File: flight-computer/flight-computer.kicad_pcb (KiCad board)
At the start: 2 copper layers, 25.4 x 50.8 mm, 29 parts, among them J1 USB_C_Receptacle_USB2.0_16P, J2 MEM2067-02-180-00-A, Q1 DMN3404L, Q2 DMN3404L, SW1 Reset, SW2 Boot, U1 LMR51420X, U2 ESP32-S3-WROOM-1, U3 LSM6DSO32TR

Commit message: more routing and laying out of board
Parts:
- removed J2: MEM2067-02-180-00-A, Library:CONN_MEM2067-02-180-00-A_GCT
- removed REF**: JST_ZE_S06B-ZESK-2D_1x06_P1.50mm_Horizontal, Connector_JST:JST_ZE_S06B-ZESK-2D_1x06_P1.50mm_Horizontal
- added J4: Conn_01x06_Pin, Connector_JST:JST_ZH_B5B-ZR-SM4-TF_1x05-1MP_P1.50mm_Vertical, F.Cu at (153.9, 89.5)
- added J5: Conn_01x06_Pin, Connector_JST:JST_ZH_B5B-ZR-SM4-TF_1x05-1MP_P1.50mm_Vertical, F.Cu at (135.6, 89.4)
- added J6: Power Connector, TerminalBlock:TerminalBlock_Xinya_XY308-2.54-2P_1x02_P2.54mm_Horizontal, F.Cu at (134.4, 108.5)
- added J7: Micro_SD_Card, Library:CONN_MEM2067-02-180-00-A_GCT, B.Cu at (144.9, 113.1)
- J3: value ~ -> Conn_01x02_Pin; footprint Library:XT30_90 -> TerminalBlock:TerminalBlock_Xinya_XY308-2.54-2P_1x02_P2.54mm_Horizontal
- R5, R6, U2: moved to B.Cu
- moved H3 69.0 mm to (135.6, 126.5)
- moved J3 63.7 mm to (154.7, 111.2), turned to 90 degrees
- moved H1 48.1 mm to (135.6, 103.2)
- moved H4 48.0 mm to (154.0, 126.5)
- moved H2 46.5 mm to (154.0, 103.2)
- moved R1 28.9 mm to (151.5, 82.0), turned to 90 degrees
- moved R4 25.5 mm to (163.8, 116.8)
- moved SW1 23.4 mm to (143.0, 82.0), turned to 0 degrees
- moved SW2 21.0 mm to (143.0, 85.5), turned to 180 degrees
- moved J1 15.2 mm to (144.9, 127.0)
- moved U3 12.8 mm to (146.5, 94.5)
- moved C6 11.6 mm to (149.5, 96.2), turned to -90 degrees
- moved D1 10.9 mm to (141.0, 120.8)
- moved R6 9.86 mm to (146.6, 125.4), turned to -90 degrees
- moved C5 6.40 mm to (144.8, 97.2), turned to 180 degrees
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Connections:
- H1 pad 1: unconnected-(H1-Pad1) -> GND
- H2 pad 1: unconnected-(H2-Pad1) -> GND
- H3 pad 1: unconnected-(H3-Pad1) -> GND
- H4 pad 1: unconnected-(H4-Pad1) -> GND
- J3 pad 1: (no net) -> Remote Start 2 EN
- J3 pad 2: (no net) -> Remote Start 1 EN
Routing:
- net USB_D-: track 0.00 -> 32.7 mm, vias 0 -> 1
- net USB_D+: track 0.00 -> 31.6 mm, vias 0 -> 1
- net Net-(U2-IO0): track 0.00 -> 14.0 mm, vias 0 -> 1
- net Net-(U2-EN): track 0.00 -> 6.50 mm
- net +3.3V: track 0.00 -> 5.85 mm, vias 0 -> 1
- net Net-(J1-CC2): track 0.00 -> 1.91 mm, vias 0 -> 1
- net Net-(J1-CC1): track 0.00 -> 1.91 mm, vias 0 -> 1
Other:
- board size 25.4 x 50.8 mm -> 25.4 x 51.5 mm
- board text added: "BOOT"
- board text added: "RST"

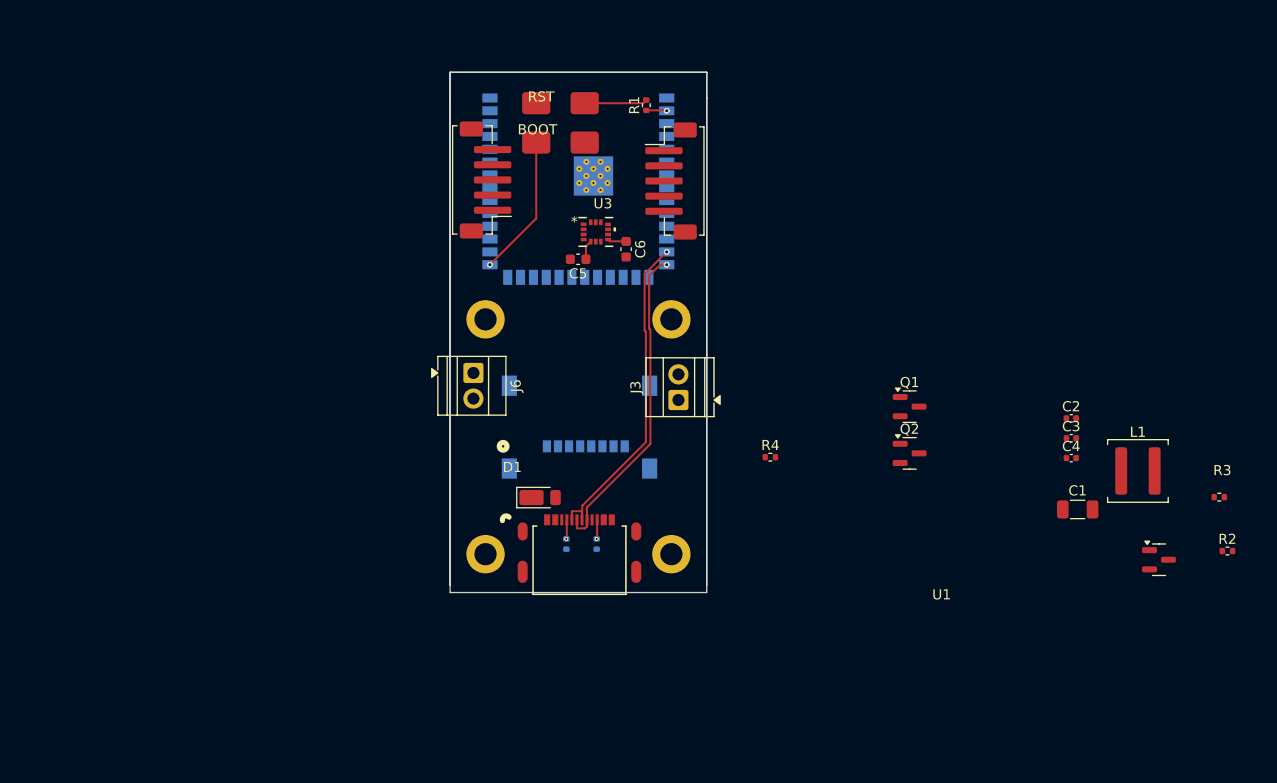
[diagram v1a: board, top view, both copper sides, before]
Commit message: some more routing for the esp board
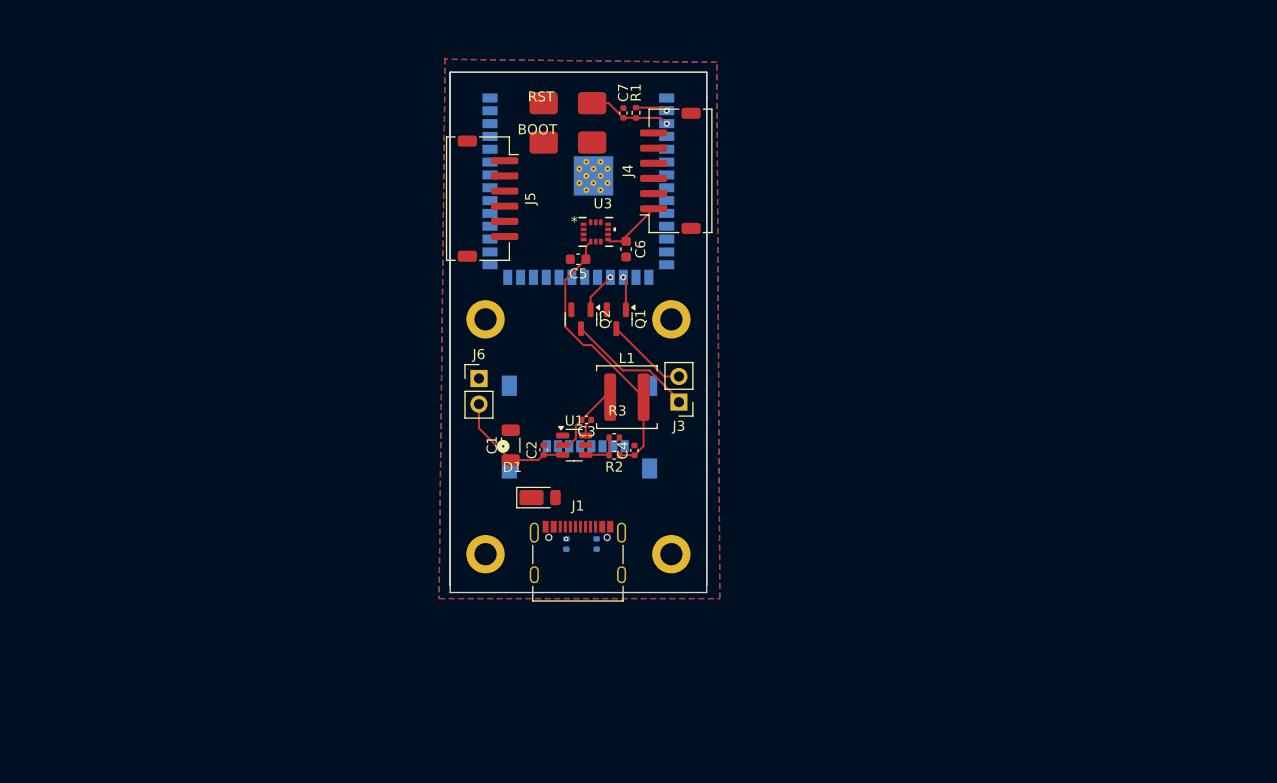
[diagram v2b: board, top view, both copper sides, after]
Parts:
- removed R4: 1M, Resistor_SMD:R_0402_1005Metric
- added C7: 1uF, Capacitor_SMD:C_0402_1005Metric, F.Cu at (149.2, 82.8)
- J1: footprint Library:CONN_USB4500_GCT -> Connector_USB:USB_C_Receptacle_Palconn_UTC16-G
- J3, J6: footprint TerminalBlock:TerminalBlock_Xinya_XY308-2.54-2P_1x02_P2.54mm_Horizontal -> Connector_PinHeader_2.54mm:PinHeader_1x02_P2.54mm_Vertical
- J4, J5: footprint Connector_JST:JST_ZH_B5B-ZR-SM4-TF_1x05-1MP_P1.50mm_Vertical -> Connector_JST:JST_ZH_S6B-ZR-SM4A-TF_1x06-1MP_P1.50mm_Horizontal
- R1: value 100k -> 10k
- U1: footprint Package_TO_SOT_SMD:SOT-23 -> Package_TO_SOT_SMD:SOT-23-6
- moved R2 61.4 mm to (148.3, 116.7), turned to 180 degrees
- moved R3 60.2 mm to (148.3, 114.9)
- moved U1 59.0 mm to (144.4, 115.7)
- moved C1 56.5 mm to (138.1, 115.7), turned to 90 degrees
- moved C2 52.3 mm to (141.3, 116.1), turned to 90 degrees
- moved L1 51.1 mm to (149.6, 110.9)
- moved C3 48.0 mm to (145.6, 113.2), turned to 180 degrees
- moved C4 43.3 mm to (150.3, 116.2), turned to 90 degrees
- moved Q2 35.1 mm to (145.0, 103.2), turned to -90 degrees
- moved Q1 30.3 mm to (148.5, 103.2), turned to -90 degrees
- moved J5 1.87 mm to (135.8, 91.2), turned to -90 degrees
- moved R1 1.26 mm to (150.5, 82.7), turned to -90 degrees
- moved J4 1.01 mm to (153.9, 88.5), turned to 90 degrees
- moved J1 0.81 mm to (144.7, 126.2)
- moved J6 0.78 mm to (134.9, 109.1), turned to 0 degrees
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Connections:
- J4 pad 1: unconnected-(J4-Pin_1-Pad1) -> +3.3V
- J4 pad 2: unconnected-(J4-Pin_2-Pad2) -> GND
- J4 pad 3: unconnected-(J4-Pin_3-Pad3) -> FIN_CS4
- J4 pad 4: unconnected-(J4-Pin_4-Pad4) -> FIN_CS3
- J4 pad 5: unconnected-(J4-Pin_5-Pad5) -> FIN_CS2
- J5 pad 1: unconnected-(J5-Pin_1-Pad1) -> FIN_RST
- J5 pad 2: unconnected-(J5-Pin_2-Pad2) -> FIN_DRDY
- J5 pad 3: unconnected-(J5-Pin_3-Pad3) -> FIN_CLK
- J5 pad 4: unconnected-(J5-Pin_4-Pad4) -> FIN_MOSI
- J5 pad 5: unconnected-(J5-Pin_5-Pad5) -> FIN_MISO
- U2 pad 17: unconnected-(U2-IO9-Pad17) -> Remote Start 1
- U2 pad 18: unconnected-(U2-IO10-Pad18) -> Remote Start 2
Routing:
- net USB_D-: track 32.7 -> 0.00 mm, vias 1 -> 0
- net USB_D+: track 31.6 -> 0.00 mm, vias 1 -> 0
- net +3.3V: track 5.85 -> 37.1 mm
- net Net-(U2-IO0): track 14.0 -> 0.00 mm, vias 1 -> 0
- net Remote Start 2 EN: track 0.00 -> 12.8 mm
- net VBUS: track 0.00 -> 12.2 mm
- net Remote Start 1 EN: track 0.00 -> 8.16 mm
- net Net-(U1-SW): track 0.00 -> 7.43 mm
- net Net-(U1-FB): track 0.00 -> 4.09 mm
- net Remote Start 2: track 0.00 -> 4.02 mm, vias 0 -> 1
- net Remote Start 1: track 0.00 -> 3.32 mm, vias 0 -> 1
- net Net-(J1-CC2): track 1.91 -> 0.00 mm, vias 1 -> 0
- net Net-(J1-CC1): track 1.91 -> 0.00 mm
- net Net-(U1-CB): track 0.00 -> 1.79 mm
- net Net-(U2-EN): track 6.50 -> 8.22 mm, vias 0 -> 1
- added copper zone on B.Cu, net GND
- added copper zone on F.Cu, net GND

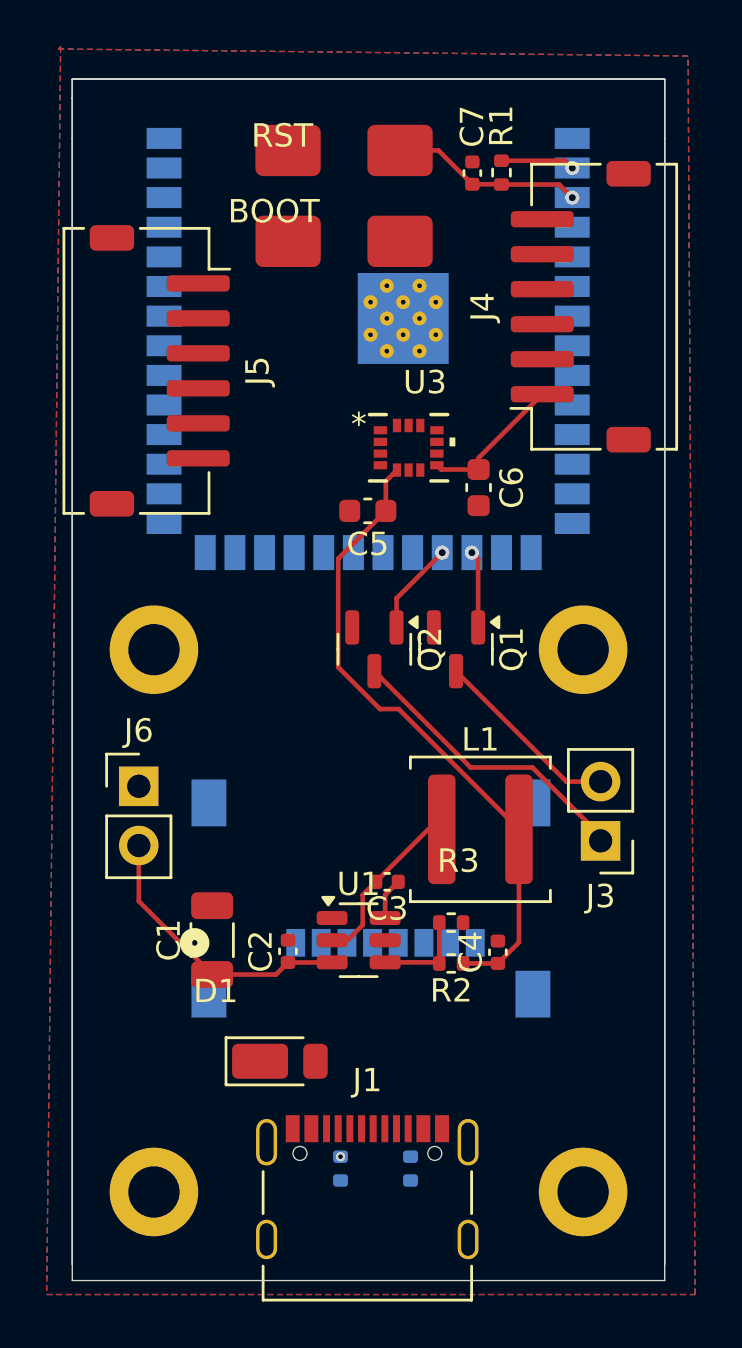
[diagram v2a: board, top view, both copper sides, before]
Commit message: finish general board layout. Needs some silkscreen fixing
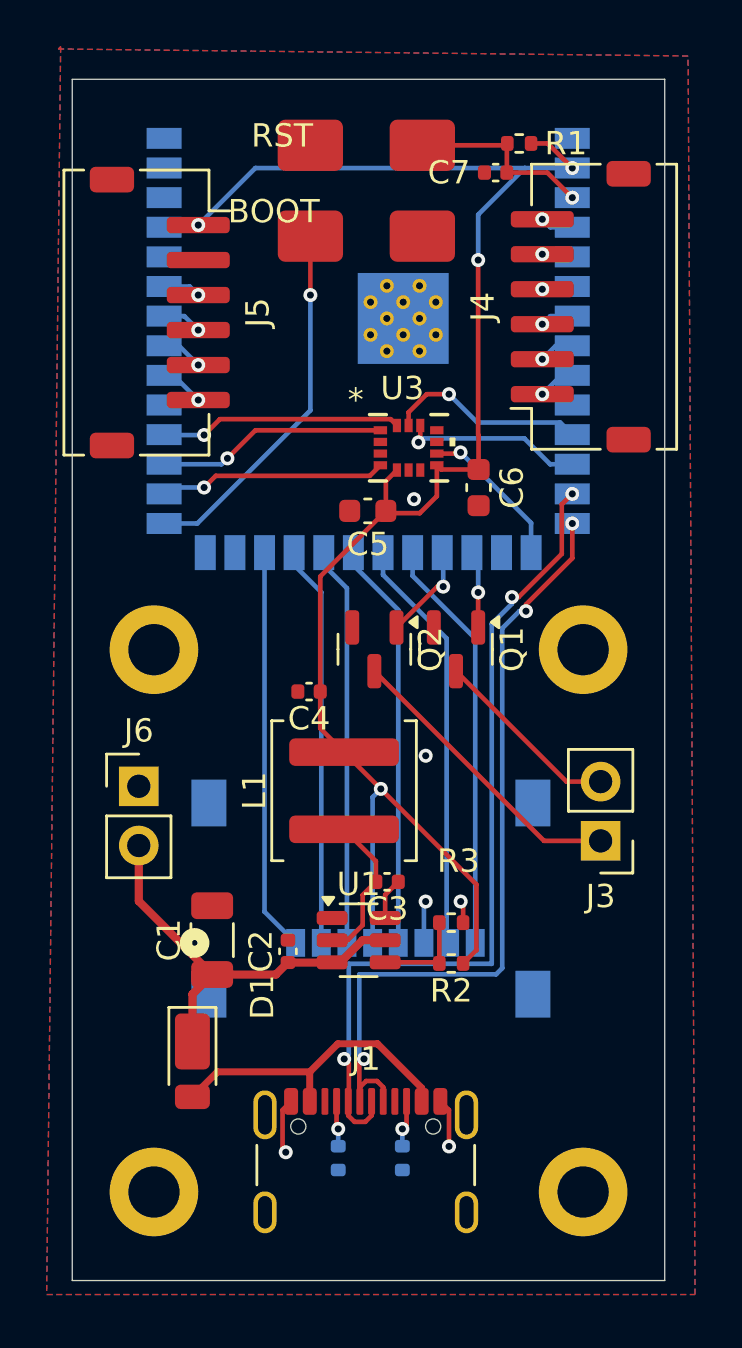
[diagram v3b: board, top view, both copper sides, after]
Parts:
- J1: footprint Connector_USB:USB_C_Receptacle_Palconn_UTC16-G -> Connector_USB:USB_C_Receptacle_GCT_USB4105-xx-A_16P_TopMnt_Horizontal
- moved C4 13.8 mm to (142.2, 105.0), turned to 180 degrees
- moved L1 6.07 mm to (143.7, 109.2), turned to 90 degrees
- moved D1 3.75 mm to (137.2, 120.8), turned to -90 degrees
- moved J5 2.50 mm to (135.8, 88.7)
- moved R1 1.46 mm to (151.2, 81.5), turned to 180 degrees
- moved C7 1.00 mm to (150.2, 82.7), turned to 180 degrees
- moved SW1 0.98 mm to (144.7, 81.8)
- moved SW2 0.98 mm to (144.7, 85.3)
- moved R6 0.57 mm to (146.2, 125.0)
- moved R5 0.46 mm to (143.5, 125.0)
- moved J1 0.07 mm to (144.7, 126.2)
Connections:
- net Remote Start 1 EN renamed Net-(J3-Pin_2)
- net Remote Start 2 EN renamed Net-(J3-Pin_1)
- J4 pad 1: +3.3V -> FIN_RST
- J4 pad 2: GND -> FIN_CLK
- J5 pad 1: FIN_RST -> +3.3V
- J5 pad 2: FIN_DRDY -> GND
- J5 pad 3: FIN_CLK -> FIN_DRDY
- J7 pad 1: unconnected-(J7-DAT2-Pad1) -> SD_DAT2
- J7 pad 2: unconnected-(J7-DAT3/CD-Pad2) -> SD_DAT3
- J7 pad 3: unconnected-(J7-CMD-Pad3) -> SD_CMD
- J7 pad 4: unconnected-(J7-VDD-Pad4) -> +3.3V
- J7 pad 5: unconnected-(J7-CLK-Pad5) -> SD_CLK
- J7 pad 6: unconnected-(J7-VSS-Pad6) -> GND
- J7 pad 7: unconnected-(J7-DAT0-Pad7) -> SD_DAT0
- J7 pad 8: unconnected-(J7-DAT1-Pad8) -> SD_DAT1
- U2 pad 11: unconnected-(U2-IO18-Pad11) -> LSM_SCK
- U2 pad 12: unconnected-(U2-IO8-Pad12) -> LSM_CS
- U2 pad 15: unconnected-(U2-IO3-Pad15) -> LSM_INT2
- U2 pad 19: unconnected-(U2-IO11-Pad19) -> SD_DAT1
- U2 pad 20: unconnected-(U2-IO12-Pad20) -> SD_DAT0
- U2 pad 21: unconnected-(U2-IO13-Pad21) -> SD_CLK
- U2 pad 22: unconnected-(U2-IO14-Pad22) -> SD_CMD
- U2 pad 23: unconnected-(U2-IO21-Pad23) -> SD_DAT3
- U2 pad 24: unconnected-(U2-IO47-Pad24) -> SD_DAT2
- U2 pad 28: unconnected-(U2-IO35-Pad28) -> LSM_INT1
- U2 pad 29: unconnected-(U2-IO36-Pad29) -> LSM_MISO
- U2 pad 30: unconnected-(U2-IO37-Pad30) -> LSM_MOSI
- U2 pad 32: unconnected-(U2-IO39-Pad32) -> FIN_SCK
- U2 pad 33: unconnected-(U2-IO40-Pad33) -> FIN_MISO
- U2 pad 34: unconnected-(U2-IO41-Pad34) -> FIN_MOSI
- U2 pad 35: unconnected-(U2-IO42-Pad35) -> FIN_DRDY
- U2 pad 4: unconnected-(U2-IO4-Pad4) -> FIN_CS1
- U2 pad 5: unconnected-(U2-IO5-Pad5) -> FIN_CS2
- U2 pad 6: unconnected-(U2-IO6-Pad6) -> FIN_CS3
- U2 pad 7: unconnected-(U2-IO7-Pad7) -> FIN_CS4
- U2 pad 8: unconnected-(U2-IO15-Pad8) -> FIN_CLK
- U2 pad 9: unconnected-(U2-IO16-Pad9) -> FIN_RST
- U3 pad 13: LSM_SCLK -> LSM_SCK
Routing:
- net USB_D-: track 0.00 -> 36.4 mm, vias 0 -> 3
- net USB_D+: track 0.00 -> 34.8 mm, vias 0 -> 3
- net +3.3V: track 37.1 -> 71.0 mm, vias 1 -> 4
- net SD_DAT0: track 0.00 -> 17.9 mm
- net SD_DAT1: track 0.00 -> 17.8 mm
- net SD_CLK: track 0.00 -> 17.5 mm
- net SD_DAT2: track 0.00 -> 17.3 mm
- net SD_DAT3: track 0.00 -> 17.2 mm
- net SD_CMD: track 0.00 -> 17.1 mm
- net Net-(U2-IO0): track 0.00 -> 15.7 mm, vias 0 -> 1
- net Net-(D1-A): track 0.00 -> 13.4 mm
- net LSM_MOSI: track 0.00 -> 10.4 mm, vias 0 -> 1
- net LSM_MISO: track 0.00 -> 9.88 mm, vias 0 -> 1
- net LSM_INT1: track 0.00 -> 9.78 mm, vias 0 -> 1
- net LSM_SCK: track 0.00 -> 8.62 mm, vias 0 -> 1
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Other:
- outline, holes or cut-outs redrawn

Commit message: switch out inductor and some caps
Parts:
- C5, C6: footprint Capacitor_SMD:C_0603_1608Metric -> Capacitor_SMD:C_0402_1005Metric
- L1: value 8.2uH -> 6.8uH; footprint Inductor_SMD:L_Coilcraft_XAL5050-XXX -> Library:IND_EXLA1V0505-220-R_EAT
- moved C6 0.25 mm to (149.5, 96.0)
- moved C5 0.23 mm to (145.0, 97.2)
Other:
- board text added: "+"
- board text added: "-"
